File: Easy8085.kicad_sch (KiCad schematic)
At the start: 31 parts, among them J1 5V Power, J2 Expansion, J3 FTDI, SW1 RESET, U1 8085, U2 74LS139, U3 74LS573, U4 CY62256, U5 X28256, U6 8251A, U7 74LS90, Y1 6.144M

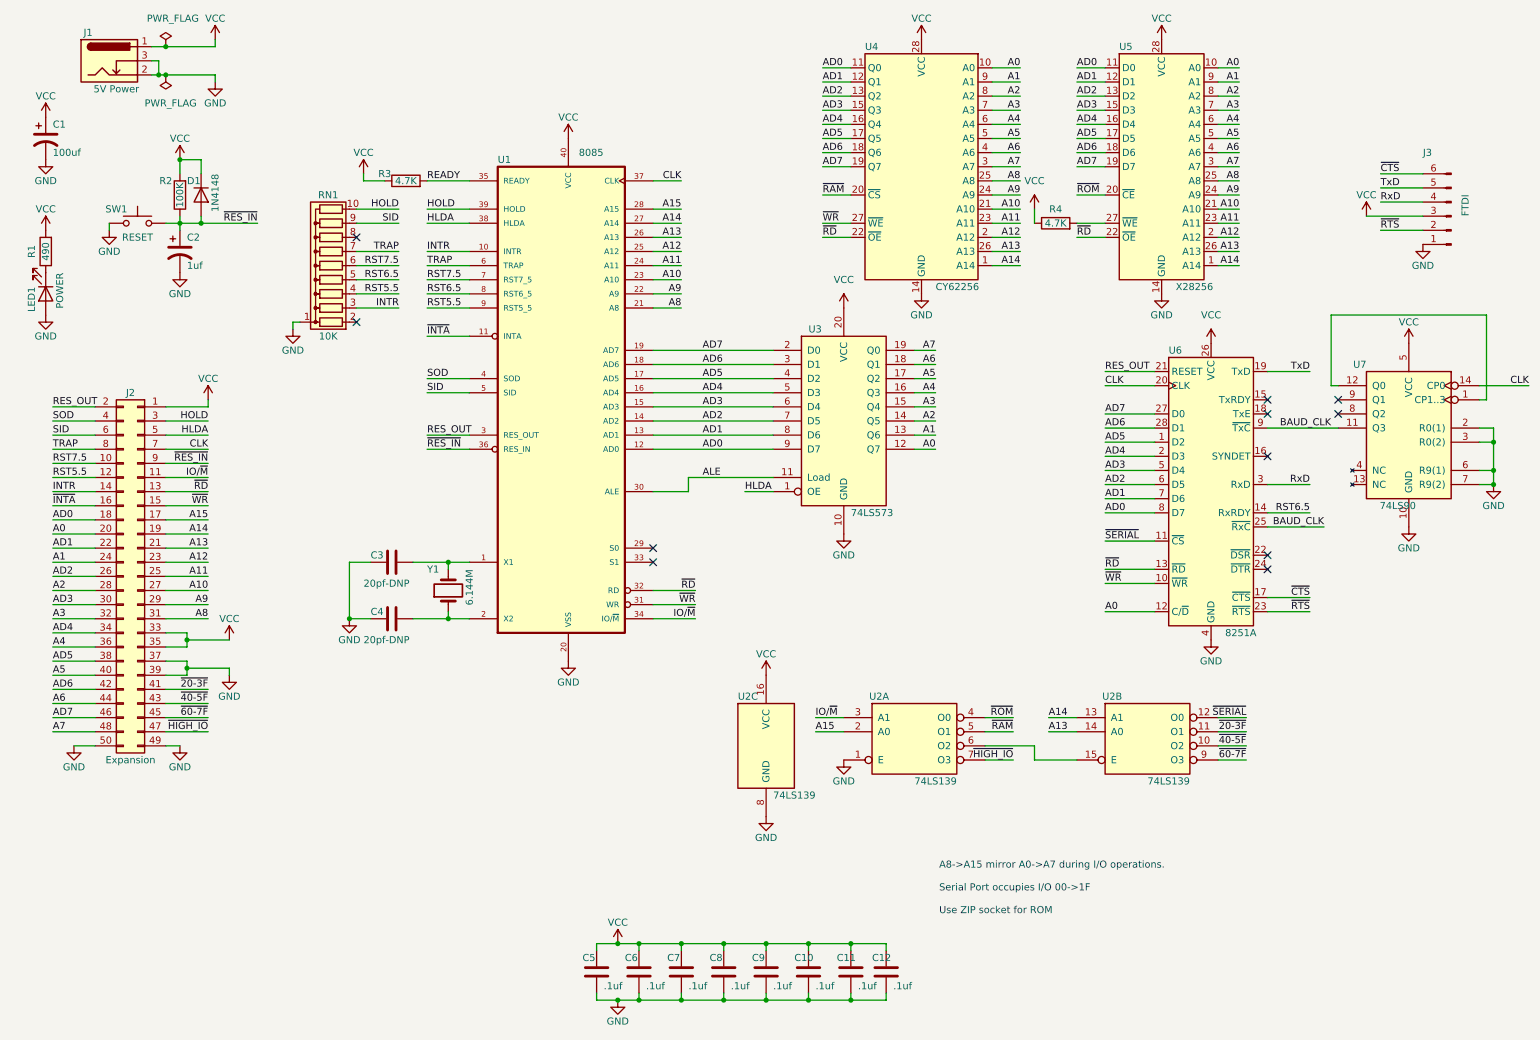
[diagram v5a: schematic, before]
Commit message: Fixed errors in PCB layout
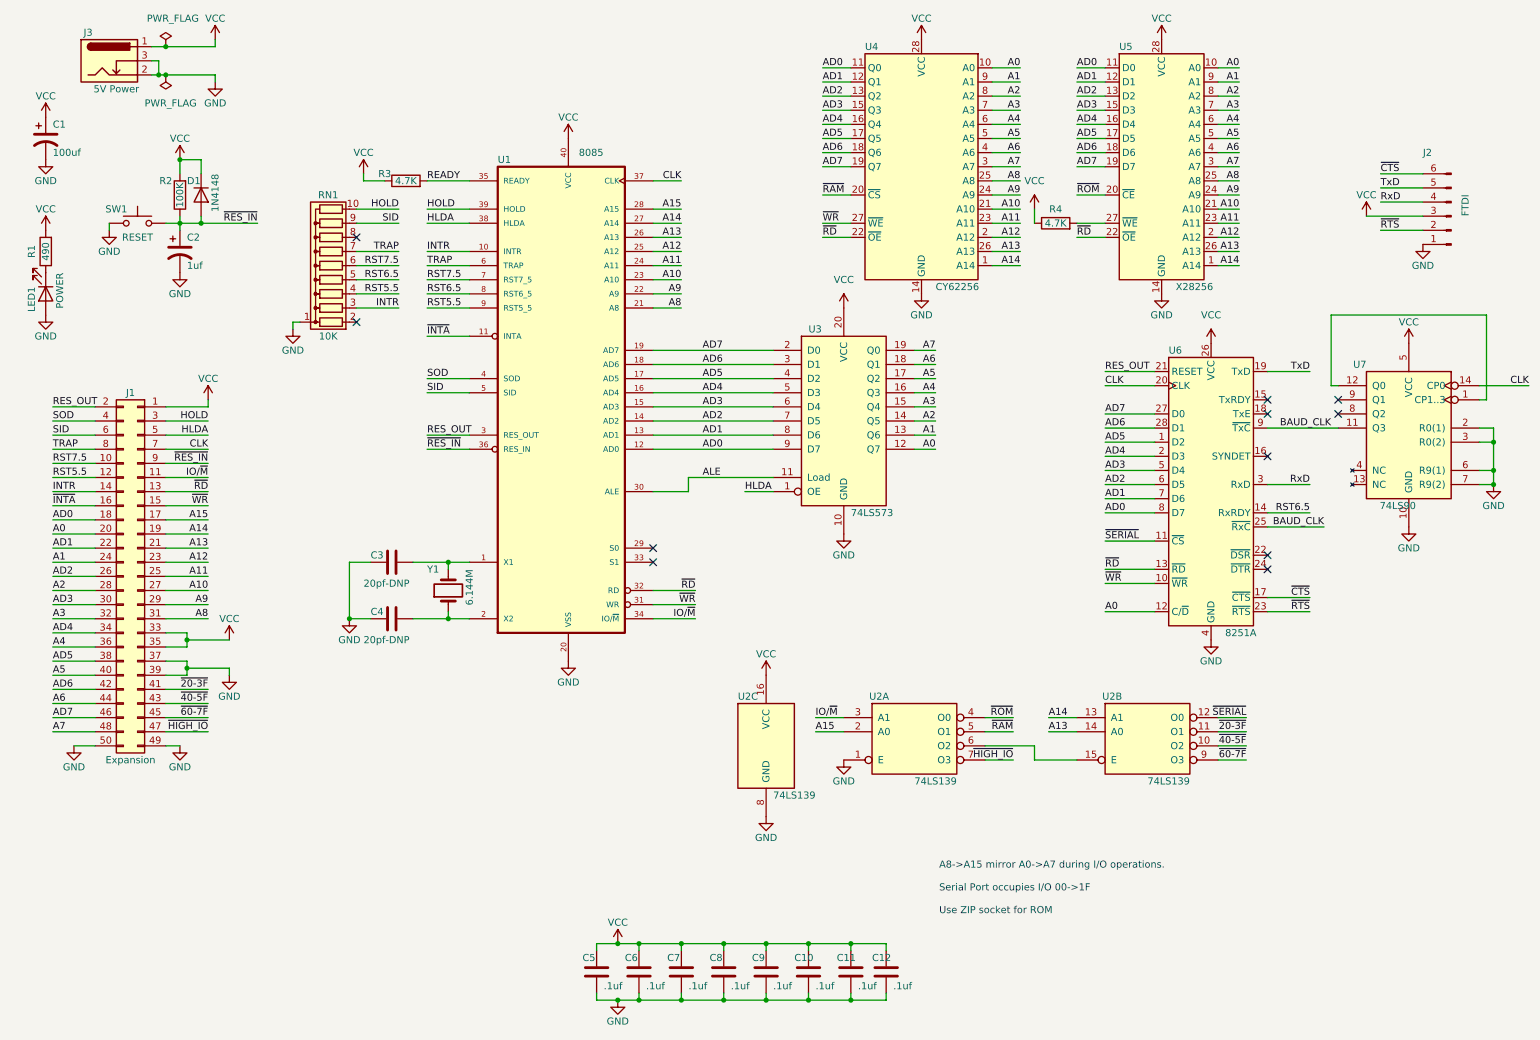
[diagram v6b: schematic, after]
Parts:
- renumbered J2 to J1, J3 to J2, J1 to J3
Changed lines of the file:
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@@
   (symbol (lib_id "Connector:Barrel_Jack_Switch") (at 29.21 22.86 0) (unit 1)
     (in_bom yes) (on_board yes)
-    (property "Reference" "J1" (id 0) (at 25.4 17.78 0))
+    (property "Reference" "J3" (id 0) (at 25.4 17.78 0))
     (property "Value" "5V Power" (id 1) (at 30.48 27.94 0))
     (property "Footprint" "Connector_BarrelJack:BarrelJack_GCT_DCJ200-10-A_Horizontal" (id 2) (at 30.48 23.876 0)
@@
   (symbol (lib_id "Connector_Generic:Conn_02x25_Odd_Even") (at 34.29 115.57 0) (mirror y) (unit 1)
     (in_bom yes) (on_board yes)
-    (property "Reference" "J2" (id 0) (at 33.02 82.55 0))
+    (property "Reference" "J1" (id 0) (at 33.02 82.55 0))
     (property "Value" "Expansion" (id 1) (at 33.02 148.59 0))
     (property "Footprint" "Connector_PinHeader_2.54mm:PinHeader_2x25_P2.54mm_Vertical" (id 2) (at 34.29 115.57 0)
@@
   (symbol (lib_id "Connector:Conn_01x06_Male") (at 270.51 50.8 180) (unit 1)
     (in_bom yes) (on_board yes)
-    (property "Reference" "J3" (id 0) (at 265.43 39.37 0)
+    (property "Reference" "J2" (id 0) (at 265.43 39.37 0)
       (effects (font (size 1.27 1.27)) (justify right))
     )
@@
       (reference "D1") (unit 1) (value "1N4148") (footprint "Diode_THT:D_DO-35_SOD27_P7.62mm_Horizontal")
     )
+    (path "/e0d0ef9a-cc29-45a5-ba6f-b69ca3458fa1"
+      (reference "J1") (unit 1) (value "Expansion") (footprint "Connector_PinHeader_2.54mm:PinHeader_2x25_P2.54mm_Vertical")
+    )
+    (path "/f776cadd-b706-4302-a69b-6276a2ad15e2"
+      (reference "J2") (unit 1) (value "FTDI") (footprint "Connector_PinSocket_2.54mm:PinSocket_1x06_P2.54mm_Horizontal")
+    )
     (path "/c6651a2e-0abb-4c39-b8a0-56694b75a049"
-      (reference "J1") (unit 1) (value "5V Power") (footprint "Connector_BarrelJack:BarrelJack_GCT_DCJ200-10-A_Horizontal")
-    )
-    (path "/e0d0ef9a-cc29-45a5-ba6f-b69ca3458fa1"
-      (reference "J2") (unit 1) (value "Expansion") (footprint "Connector_PinHeader_2.54mm:PinHeader_2x25_P2.54mm_Vertical")
-    )
-    (path "/f776cadd-b706-4302-a69b-6276a2ad15e2"
-      (reference "J3") (unit 1) (value "FTDI") (footprint "Connector_PinSocket_2.54mm:PinSocket_1x06_P2.54mm_Horizontal")
+      (reference "J3") (unit 1) (value "5V Power") (footprint "Connector_BarrelJack:BarrelJack_GCT_DCJ200-10-A_Horizontal")
     )
     (path "/dda4c11a-8292-40fe-b319-7fd3a9991729"

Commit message: Fixed mounting holes and re-annotated schematic
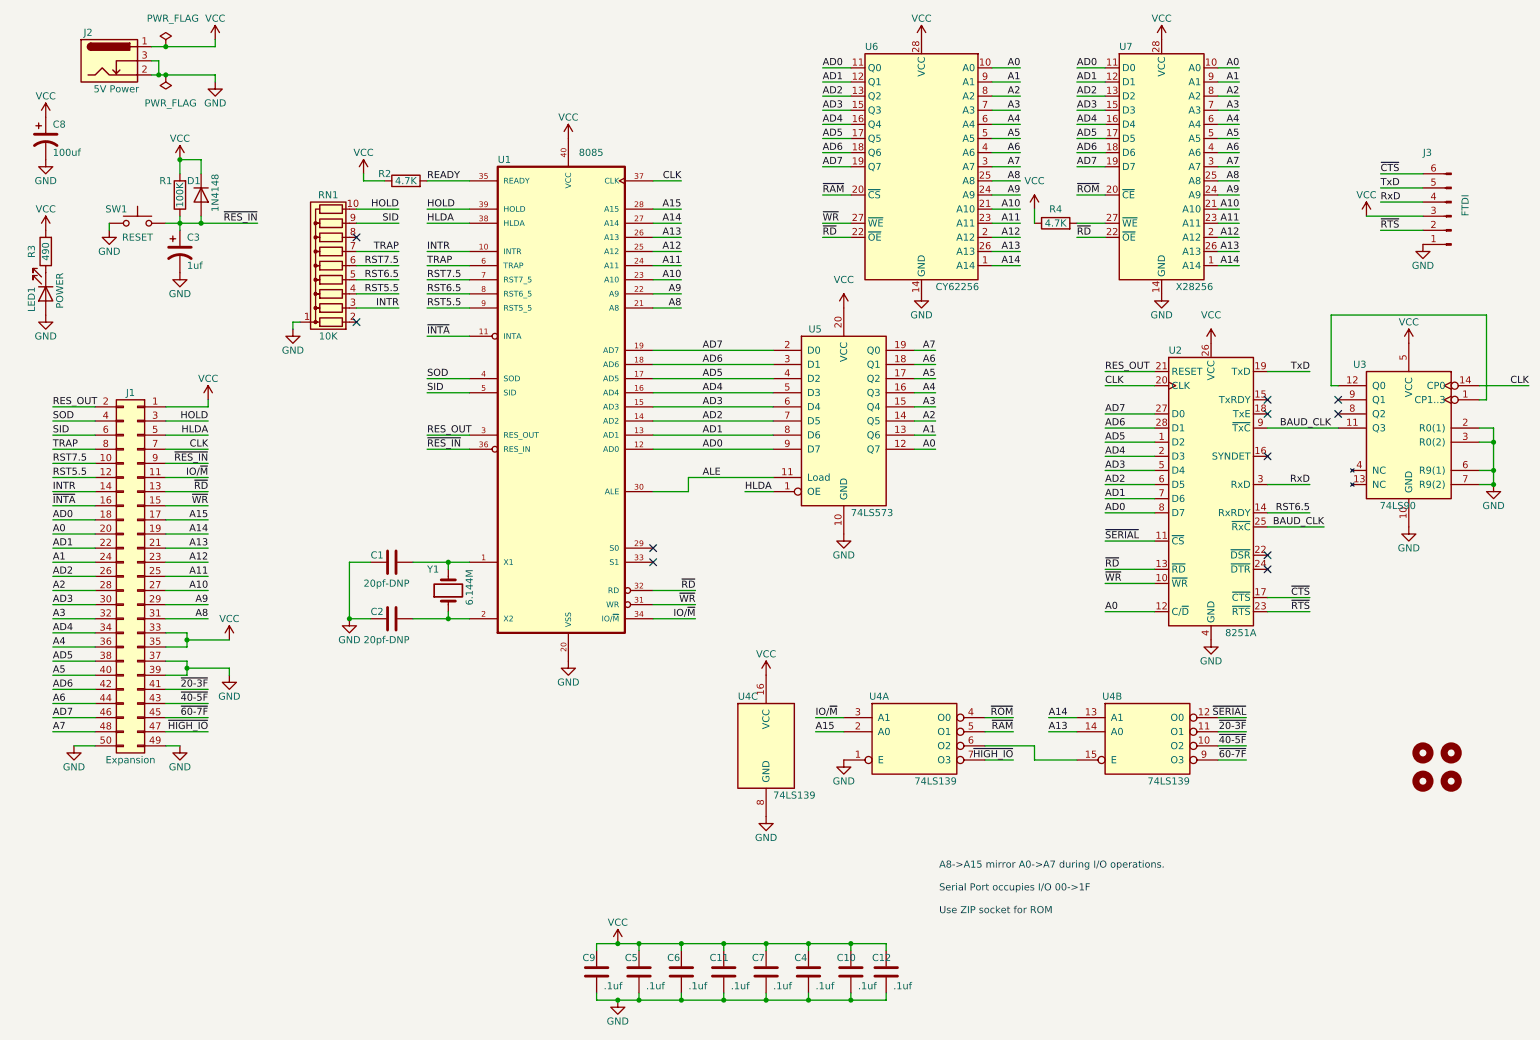
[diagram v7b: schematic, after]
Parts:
- added H1, H2, H3, H4: MountingHole, MountingHole:MountingHole_2.7mm_M2.5, symbol Mechanical:MountingHole
- renumbered C3 to C1, C11 to C10, C8 to C11, C4 to C2, C2 to C3, C10 to C4, C6 to C5, C7 to C6, C9 to C7, C1 to C8, C5 to C9, J3 to J2, J2 to J3, R2 to R1, R3 to R2, R1 to R3, U6 to U2, U7 to U3, U2 to U4, U3 to U5, U4 to U6, U5 to U7

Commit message: Finished layout
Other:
- note added: "A8->A15 mirror A0->A7 during I/O operations. Serial Port occupies I/O 00->1F Use ZIF socket for ROM Do not populate the 20pf caps unless necessary."
- note added: "Mounting Holes"
- note removed: "A8->A15 mirror A0->A7 during I/O operations. Serial Port occupies I/O 00->1F Use ZIP socket for ROM"
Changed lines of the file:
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@@
     (stroke (width 0) (type default) (color 0 0 0 0))
   )
-  (text "A8->A15 mirror A0->A7 during I/O operations.\n\nSerial Port occupies I/O 00->1F\n\nUse ZIP socket for ROM"
-    (at 178.435 176.53 0)
+  (text "A8->A15 mirror A0->A7 during I/O operations.\n\nSerial Port occupies I/O 00->1F\n\nUse ZIF socket for ROM\n\nDo not populate the 20pf caps unless necessary."
+    (at 178.435 180.975 0)
     (effects (font (size 1.27 1.27)) (justify left bottom))
   )
+  (text "Mounting Holes" (at 261.62 144.78 0)
+    (effects (font (size 1.27 1.27)) (justify left bottom))
+  )
